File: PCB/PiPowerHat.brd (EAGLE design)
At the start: 65 x 56 mm, 29 parts, among them IC1 7805T, K1 PIN20X2, U1 EEPROM24, U2 INA219AIDCNRSOIC, U4 DS18B20

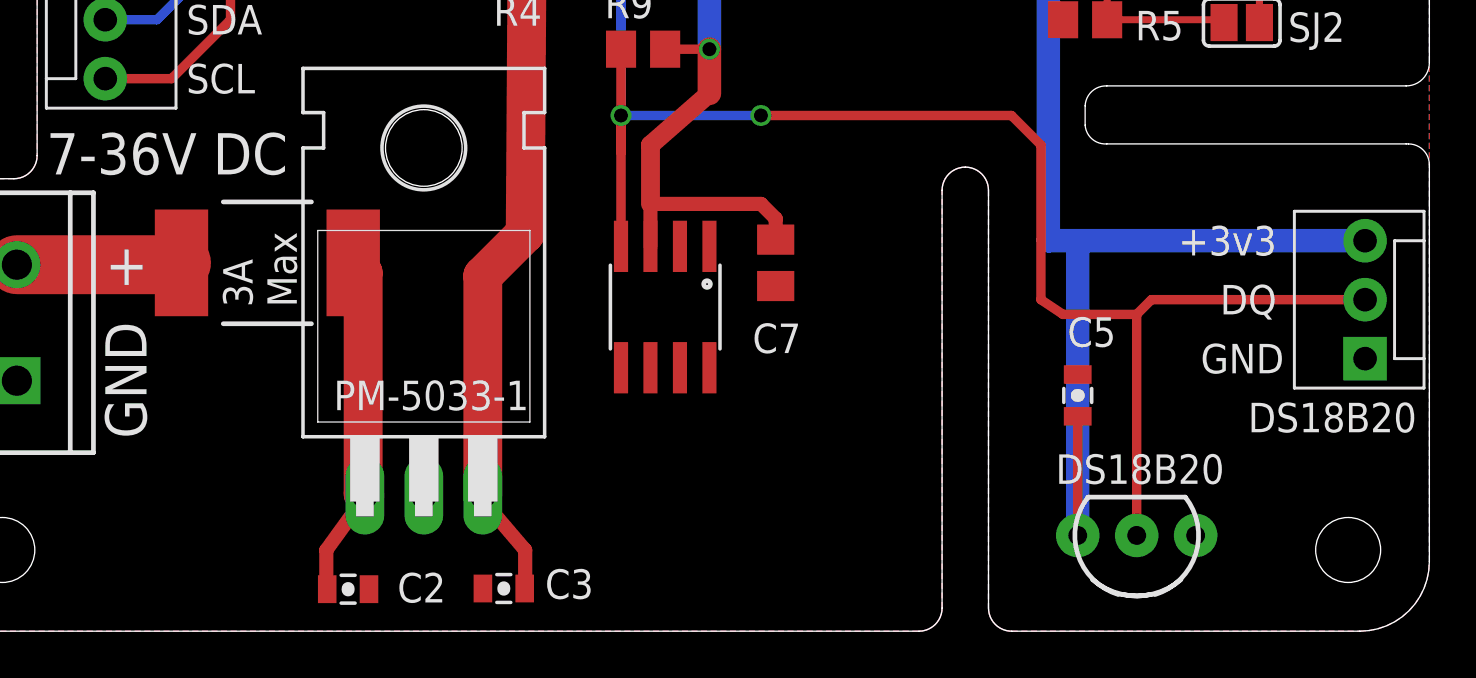
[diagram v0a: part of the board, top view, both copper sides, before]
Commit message: Corrected dimension measurements to be on the measurements layer, not dimensions.
Added Version and name/date.

Printed schema and PCB to PDFs

Added readme.
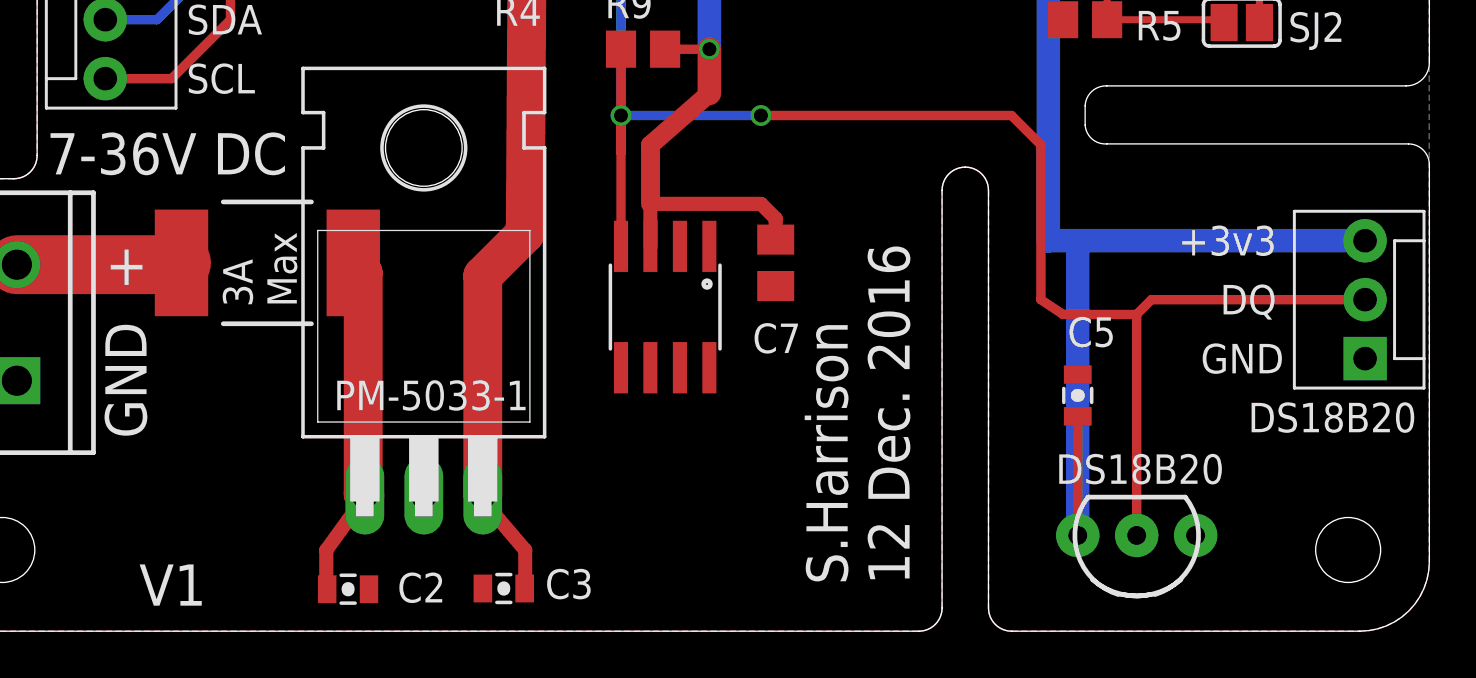
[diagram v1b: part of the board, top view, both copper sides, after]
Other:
- outline, holes or cut-outs redrawn
- board text added: "S.Harrison 12 Dec. 2016"
- board text added: "V1"
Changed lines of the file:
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@@
 <wire x1="46" y1="1" x2="47" y2="0" width="0" layer="20" curve="90"/>
 <wire x1="64" y1="23.5" x2="51.1" y2="23.5" width="0" layer="20"/>
-<wire x1="51.1" y1="21" x2="64" y2="21" width="0" layer="20"/>
+<wire x1="51.1" y1="21" x2="64.1" y2="21" width="0" layer="20"/>
 <wire x1="51.1" y1="23.5" x2="50.165" y2="22.6425" width="0" layer="20" curve="90"/>
 <wire x1="50.165" y1="22.6425" x2="50.165" y2="21.8075" width="0" layer="20"/>
@@
 <text x="48.895" y="6.35" size="1.27" layer="25">DS18B20</text>
 <wire x1="64" y1="23.5" x2="65" y2="24.5" width="0" layer="20" curve="90"/>
-<wire x1="64" y1="21" x2="64.1" y2="21" width="0" layer="20"/>
 <wire x1="64.1" y1="21" x2="65" y2="20.1" width="0" layer="20" curve="-90"/>
-<dimension x1="0" y1="53" x2="65" y2="50.6" x3="32.5" y3="61.7" textsize="1.27" layer="20" dtype="horizontal"/>
-<dimension x1="62" y1="56" x2="62" y2="0" x3="71.4" y3="28" textsize="1.27" layer="20" dtype="vertical"/>
+<dimension x1="0" y1="53" x2="65" y2="50.6" x3="32.5" y3="61.7" textsize="1.27" layer="47" dtype="horizontal"/>
+<dimension x1="62" y1="56" x2="62" y2="0" x3="71.4" y3="28" textsize="1.27" layer="47" dtype="vertical"/>
+<text x="42.6" y="2" size="1.778" layer="25" rot="R90">S.Harrison
+12 Dec. 2016</text>
+<text x="9.4" y="1.1" size="1.778" layer="25">V1</text>
 </plain>
 <attributes>

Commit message: Tidied up schematic/board with feedback from 1st build.
Added BOM.
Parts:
- R4: value 0.001 -> 0.1
- R5, R6: value 3k9 -> 10k
- renumbered U$1 to U5
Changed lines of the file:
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@@
 <attribute name="VALUE" x="29.413" y="32.5785" size="0.4064" layer="27" rot="R270"/>
 </element>
-<element name="R4" library="SparkFun-Resistors" package="2512" value="0.001" x="26.2675" y="31.5775" locked="yes" smashed="yes" rot="R270">
+<element name="R4" library="SparkFun-Resistors" package="2512" value="0.1" x="26.2675" y="31.5775" locked="yes" smashed="yes" rot="R270">
 <attribute name="PROD_ID" value="RES-12449" x="26.2675" y="31.5775" size="1.778" layer="27" rot="R270" display="off"/>
 <attribute name="NAME" x="24.6675" y="26.0925" size="1.27" layer="25"/>
@@
 <attribute name="VALUE" x="49.2125" y="6.0325" size="0.4064" layer="27" ratio="10" rot="R180"/>
 </element>
-<element name="U$1" library="DS1820-SOIC" package="DS18B20_SOIC" value="DS1820SOIC" x="32.0675" y="13.97" smashed="yes" rot="R180"/>
+<element name="U5" library="DS1820-SOIC" package="DS18B20_SOIC" value="DS1820SOIC" x="32.0675" y="13.97" smashed="yes" rot="R180"/>
 <element name="J2" library="SparkFun-Connectors" package="MOLEX-1X3" value="" x="62.23" y="11.7475" locked="yes" smashed="yes" rot="R90"/>
-<element name="R5" library="resistor" package="M0805" value="3k9" x="50.165" y="26.3525" smashed="yes">
+<element name="R5" library="resistor" package="M0805" value="10k" x="50.165" y="26.3525" smashed="yes">
 <attribute name="TOLERANCE" value="5%" x="50.165" y="26.3525" size="1.778" layer="27" display="off"/>
 <attribute name="NAME" x="52.324" y="25.4635" size="1.27" layer="25"/>
 <attribute name="VALUE" x="49.149" y="24.0665" size="1.27" layer="27"/>
 </element>
-<element name="R6" library="resistor" package="M0805" value="3k9" x="50.165" y="29.21" smashed="yes">
+<element name="R6" library="resistor" package="M0805" value="10k" x="50.165" y="29.21" smashed="yes">
 <attribute name="TOLERANCE" value="5%" x="50.165" y="29.21" size="1.778" layer="27" display="off"/>
 <attribute name="NAME" x="52.324" y="28.321" size="1.27" layer="25"/>
@@
 <contactref element="C5" pad="1"/>
 <contactref element="U4" pad="1"/>
-<contactref element="U$1" pad="GND"/>
+<contactref element="U5" pad="GND"/>
 <contactref element="J2" pad="1"/>
 <contactref element="R5" pad="1"/>
@@
 <wire x1="28.575" y1="45.4025" x2="28.575" y2="51.115" width="1.016" layer="1"/>
 <wire x1="28.575" y1="51.115" x2="28.69" y2="51.23" width="1.016" layer="1"/>
-<contactref element="U$1" pad="VCC"/>
+<contactref element="U5" pad="VCC"/>
 <contactref element="J2" pad="3"/>
 <wire x1="37.9488" y1="34.0975" x2="37.1475" y2="34.0975" width="0.8128" layer="1"/>
@@
 <signal name="GPIO4">
 <contactref element="K1" pad="7"/>
-<contactref element="U$1" pad="DQ"/>
+<contactref element="U5" pad="DQ"/>
 <wire x1="15.99" y1="51.23" x2="15.99" y2="38.3025" width="0.4064" layer="1"/>
 <wire x1="15.99" y1="38.3025" x2="16.8275" y2="37.465" width="0.4064" layer="1"/>

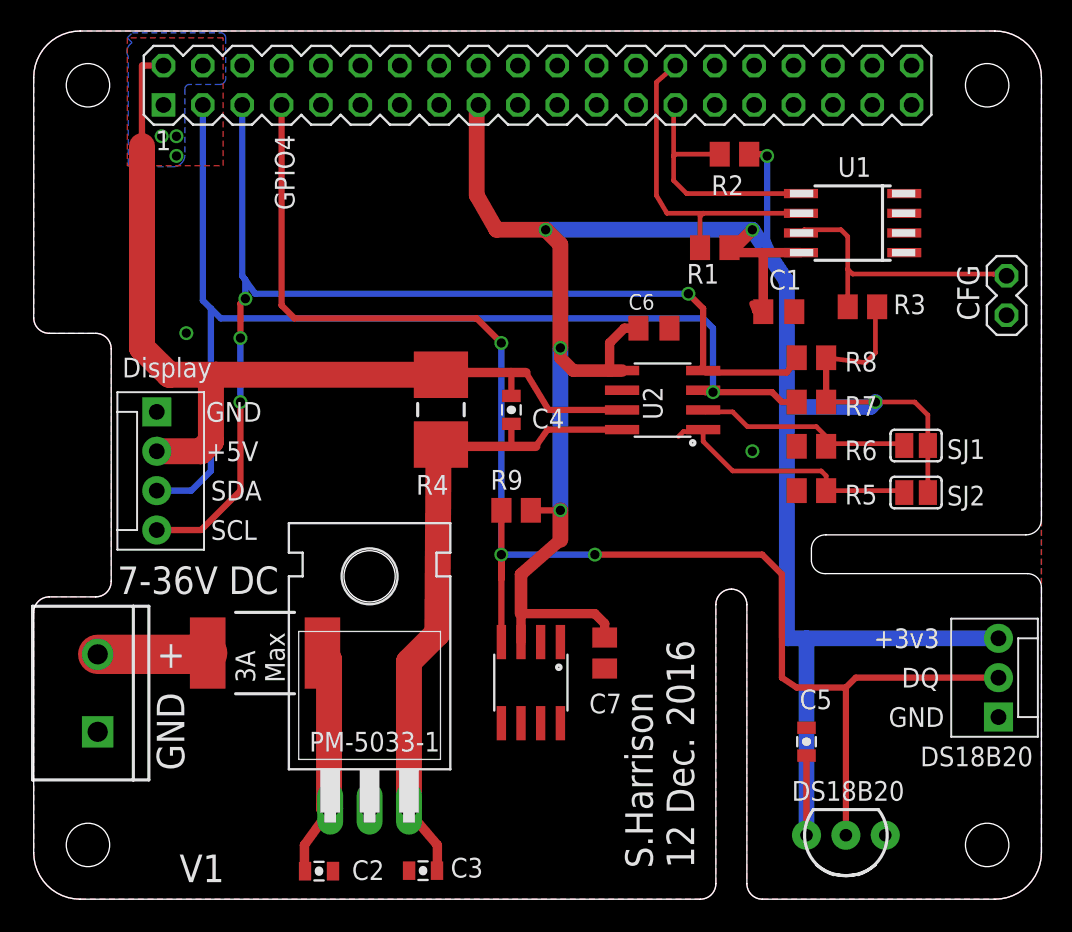
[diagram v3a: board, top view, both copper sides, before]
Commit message: Improved routing to not use bottom layer so much
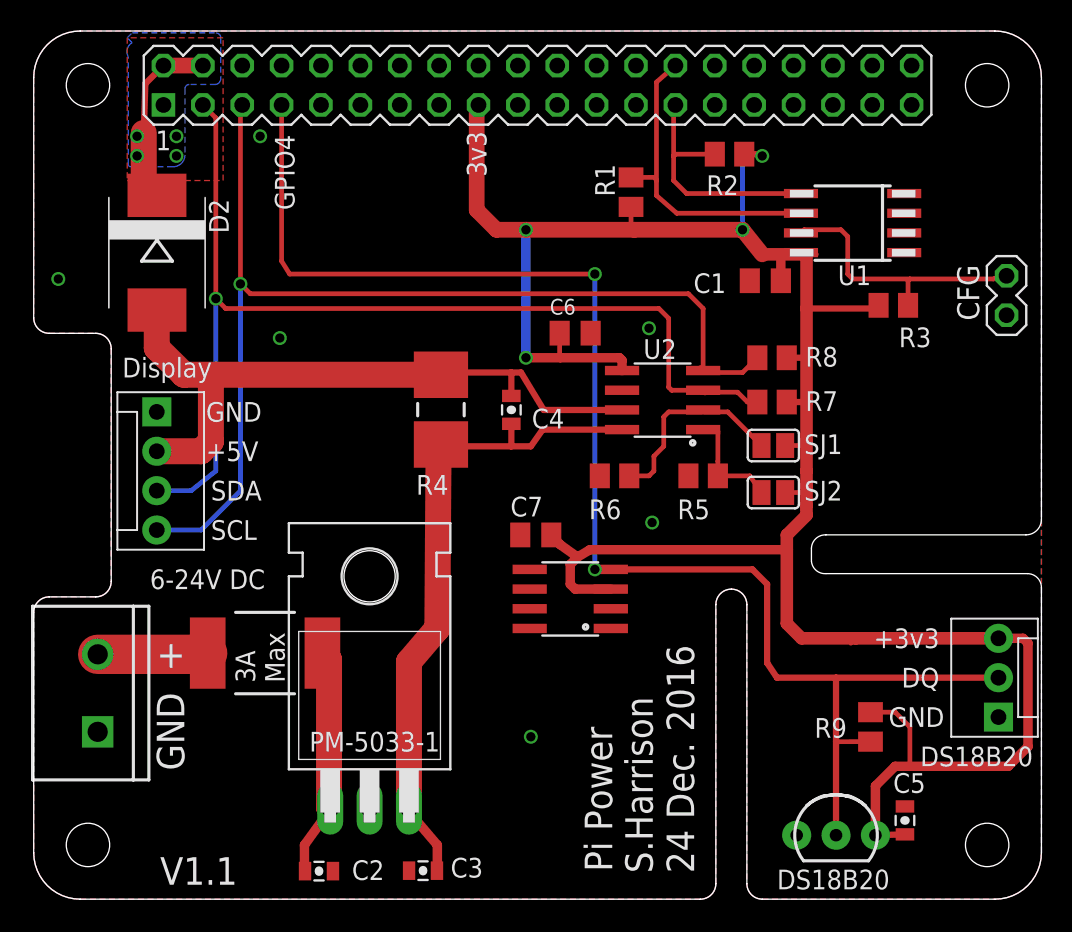
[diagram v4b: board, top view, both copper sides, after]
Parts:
- added D2: (no value), diode:SMC
- C2: value 1.0uF -> 1.0uF 50v
- moved R9 26.8 mm to (54.0, 11.1), turned to 90 degrees
- moved R6 12.8 mm to (37.5, 27.3)
- moved SJ1 9.21 mm to (47.7, 29.3)
- moved SJ2 9.21 mm to (47.7, 26.2)
- moved C7 8.82 mm to (32.4, 23.5), turned to 180 degrees
- moved C5 8.13 mm to (56.2, 5.08)
- moved R5 7.05 mm to (43.2, 27.3)
- moved R1 6.48 mm to (38.5, 45.6), turned to 270 degrees
- moved U5 5.97 mm to (34.6, 19.4), turned to 90 degrees
- moved C6 5.09 mm to (34.9, 36.5)
- moved R7 2.54 mm to (47.6, 32.1)
- moved R8 2.54 mm to (47.6, 34.9)
- moved C1 2.18 mm to (47.2, 39.9), turned to 180 degrees
- moved R3 1.99 mm to (55.4, 38.3), turned to 180 degrees
- moved U4 0.64 mm to (51.8, 4.13), turned to 0 degrees
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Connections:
- new net N$2: D2.C, K1.2, K1.4
- net +5V: now also D2.A; no longer K1.2, K1.4
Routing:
- net +5V: track 62.4 -> 44.3 mm, vias 3 -> 0
- net +3V3: track 178.1 -> 162.3 mm, vias 6 -> 4
- net N$2: track 0.00 -> 12.2 mm, vias 0 -> 4
- net N$10: track 17.4 -> 7.23 mm
- net GPIO4: track 102.7 -> 94.3 mm, vias 3 -> 2
- net SCL: track 72.8 -> 70.1 mm, vias 4 -> 1
- net SDA: track 71.4 -> 68.7 mm
- net N$9: track 14.6 -> 12.9 mm
- net ID_SC: track 21.2 -> 20.4 mm
- added copper zone on layer 1, net N$2
- added copper zone on layer 16, net N$2
- removed copper zone on layer 1, net +5V
- removed copper zone on layer 16, net +5V
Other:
- board text added: "3v3"
- board text added: "6-24V DC"
- board text added: "Pi Power"
- board text added: "S.Harrison 24 Dec. 2016"
- board text added: "V1.1"
- board text removed: "7-36V DC"
- board text removed: "S.Harrison 12 Dec. 2016"
- board text removed: "V1"

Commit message: Improved routing to increase ground plain, change IO pins used with option to select between 2 IO pins for temperature sensors.
Added OSH logo and rear LED.
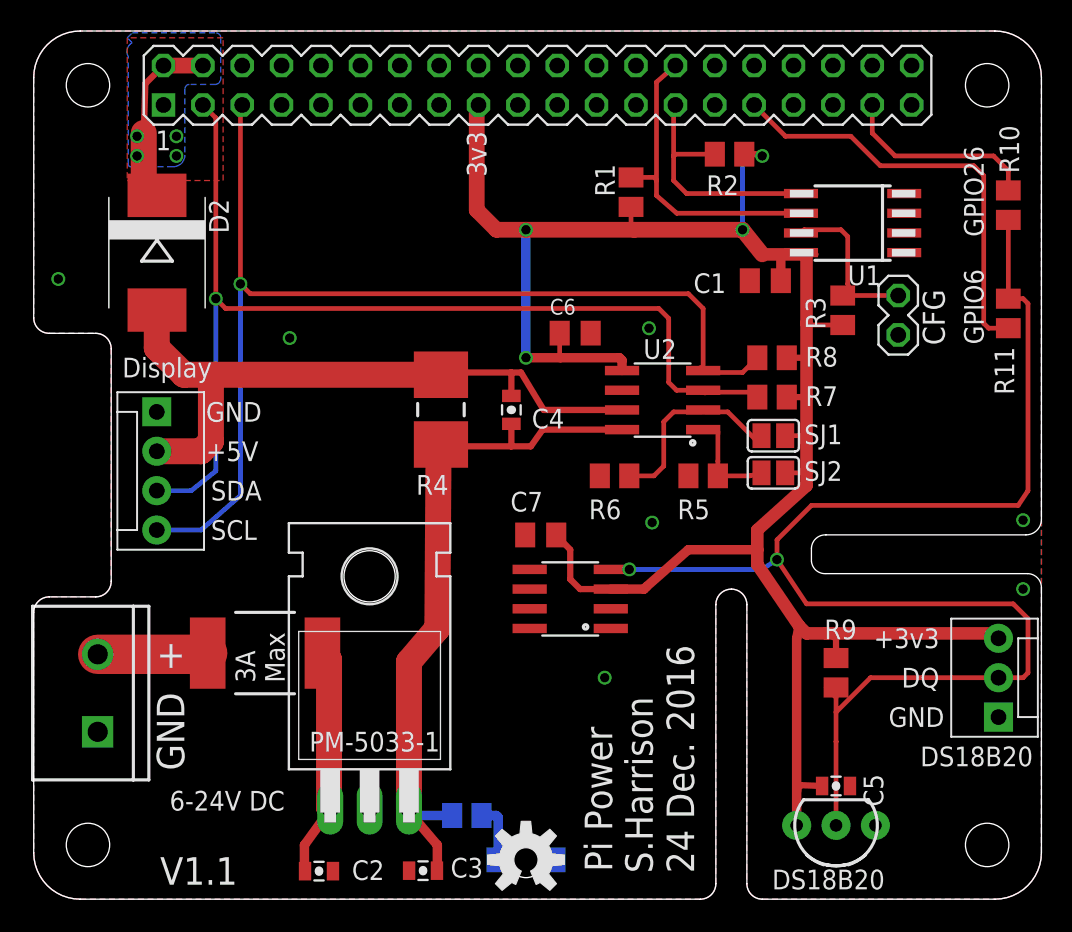
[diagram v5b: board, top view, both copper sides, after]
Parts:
- added D3: (no value), SparkFun-LED:LED-1206-BOTTOM
- added LOGO1: OSHW-LOGOM, SparkFun-Aesthetics:OSHW-LOGO-M
- added R10, R11: 0R, resistor:M0805
- added R12: 1k5, resistor:M0805
- moved CFG 7.10 mm to (55.8, 38.9)
- moved C5 4.97 mm to (51.8, 7.30), turned to 180 degrees
- moved R9 4.14 mm to (51.8, 14.6)
- moved R3 3.28 mm to (52.2, 38.0), turned to 270 degrees
- moved SJ2 1.27 mm to (47.7, 27.5)
- moved SJ1 0.64 mm to (47.7, 29.9)
- moved U4 0.63 mm to (51.8, 4.76), turned to 180 degrees
- moved C7 0.32 mm to (32.7, 23.5)
- moved R7 0.32 mm to (47.6, 32.4)
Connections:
- new net GPIO26: K1.37, R10.2
- new net GPIO6: K1.31, R11.2
- new net N$4: D3.A, R12.1
- new net TEMPERATURE: J2.2, R10.1, R11.1, R9.1, U4.2, U5.DQ
- net GND: now also D3.C
- net GPIO4: no longer J2.2, R9.1, U4.2, U5.DQ
- net VCC: now also R12.2
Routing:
- net GPIO4: track 94.3 -> 0.00 mm, vias 2 -> 0
- net TEMPERATURE: track 0.00 -> 93.2 mm, vias 0 -> 2
- net GPIO6: track 0.00 -> 27.9 mm
- net +3V3: track 162.3 -> 142.2 mm
- net GPIO26: track 0.00 -> 12.9 mm
- net N$3: track 17.9 -> 10.7 mm
- net N$4: track 0.00 -> 4.18 mm
- net VCC: track 42.6 -> 45.5 mm
- net N$10: track 7.23 -> 6.70 mm
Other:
- board text added: "GPIO26"
- board text added: "GPIO6"
- board text removed: "GPIO4"
